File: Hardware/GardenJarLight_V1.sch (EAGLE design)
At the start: 21 parts, among them IC1 TP4054_LIPO_CHARGER, M1 ARDUINO-PRO-MINI-3.3V#NP, Q1 MOSFET-PCHANNEL

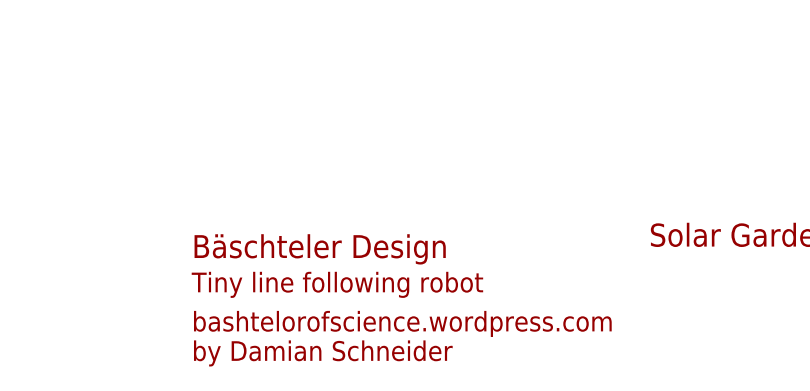
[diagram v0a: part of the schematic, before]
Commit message: updated silkscreen
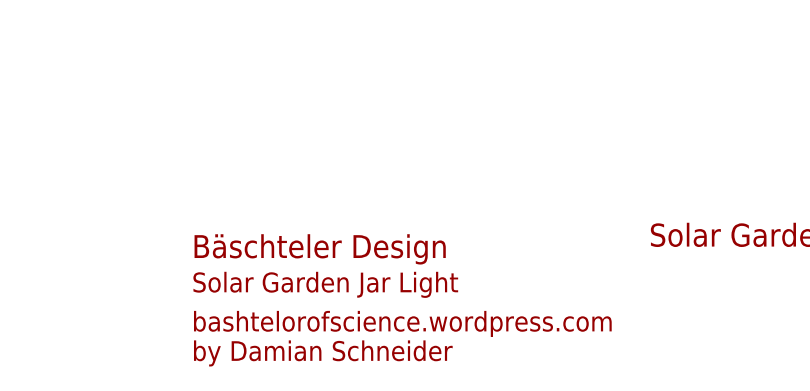
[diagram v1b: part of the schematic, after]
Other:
- note removed: "Tiny line following robot"
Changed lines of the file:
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@@
 <text x="280.67" y="7.62" size="2.1844" layer="94">bashtelorofscience.wordpress.com
 by Damian Schneider</text>
-<text x="280.67" y="15.24" size="2.1844" layer="94">Tiny line following robot</text>
+<text x="280.67" y="15.24" size="2.1844" layer="94">Solar Garden Jar Light</text>
 <text x="331.47" y="20.32" size="2.54" layer="94">Solar Garden Jar Light</text>
 <text x="302.26" y="66.04" size="1.778" layer="94">Arduino Pro Mini</text>
